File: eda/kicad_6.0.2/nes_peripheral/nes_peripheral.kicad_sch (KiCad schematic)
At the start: 126 parts, among them J1 CONN_USER, J10 CONN_JOY2, J11 CONN_JOY2_OE_SEL, J12 CONN_JOY1_OE_SEL, J13 CONN_JOY1_FC, J14 CONN_JOY1_FC_COMPATIBLE, J15 CONN_JOY1_MIC, J16 CONN_5V_RESERVE, J17 DB15_Female_JOY1, J18 DB9_Female_JOY1, J19 CONN_SOUND_IO, J2 CONN_GPIO0_DBG, J20 CONN_JOY2_FC, J21 CONN_JOY2_FC_COMPATIBLE, J22 CONN_JOY2_MIC, J23 FC_CONN, J24 CONN_CART_DBG, J25 CONN_CART_DBG, J26 DB15_Female_JOY2, J27 DB9_Female_JOY2, J28 CONN_JOY2_DBGSEL, J29 CONN_JOY1_DBGSEL, J3 CONN_GPIO1_DBG, J30 CONN_GAINSEL, J31 Screw_Terminal_SPK, J32 CONN_SPK, J33 CONN_JOY2_DBG, J34 CONN_JOY1_DBG, J4 Jack_EXT5V, J5 CONN_GPIO0_DBG, J6 CONN_GPIO1_DBG, J7 CONN_CART_OE_SEL, J8 CONN_5VSEL, J9 CONN_JOY1, U1 TXB0104PW, U10 TXB0104PW, U11 TXB0104PW, U12 TXB0104PW, U13 TXB0104PW, U14 TXB0104PW, U15 TXB0104PW, U16 TXB0104PW, U17 4021, U18 4021, U19 MAX98357, U2 TXB0104PW, U20 MAX98357, U3 TXB0104PW, U4 TXB0104PW, U5 TXB0104PW, U6 TXB0104PW, U7 TXB0104PW, U8 TXB0104PW, U9 TXB0104PW

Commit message: wip: 基板配置検討中
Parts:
- removed J13: CONN_JOY1_FC, Connector_PinSocket_2.54mm:PinSocket_2x15_P2.54mm_Vertical, symbol Connector_Generic:Conn_02x15_Odd_Even
- removed J17: DB15_Female_JOY1, Connector_Dsub:DSUB-15-HD_Female_Horizontal_P2.29x1.98mm_EdgePinOffset9.40mm, symbol Connector:DB15_Female
- removed J18: DB9_Female_JOY1, Connector_Dsub:DSUB-9_Female_Horizontal_P2.77x2.84mm_EdgePinOffset9.40mm, symbol Connector:DB9_Female
- removed J2, J5: CONN_GPIO0_DBG, Connector_PinSocket_2.54mm:PinSocket_1x20_P2.54mm_Vertical, symbol Connector_Generic:Conn_01x20
- removed J20: CONN_JOY2_FC, Connector_PinSocket_2.54mm:PinSocket_2x15_P2.54mm_Vertical, symbol Connector_Generic:Conn_02x15_Odd_Even
- removed J26: DB15_Female_JOY2, Connector_Dsub:DSUB-15-HD_Female_Horizontal_P2.29x1.98mm_EdgePinOffset9.40mm, symbol Connector:DB15_Female
- removed J27: DB9_Female_JOY2, Connector_Dsub:DSUB-9_Female_Horizontal_P2.77x2.54mm_EdgePinOffset9.40mm, symbol Connector:DB9_Female
- removed J3, J6: CONN_GPIO1_DBG, Connector_PinSocket_2.54mm:PinSocket_1x20_P2.54mm_Vertical, symbol Connector_Generic:Conn_01x20
- added H1, H2, H3: MountingHole_Pad, MountingHole:MountingHole_3.2mm_M3_Pad_TopBottom, symbol Mechanical:MountingHole_Pad
- J1: footprint Connector_PinSocket_2.54mm:PinSocket_2x06_P2.54mm_Vertical -> Connector_PinSocket_2.54mm:PinSocket_1x06_P2.54mm_Vertical; symbol Connector_Generic:Conn_02x06_Odd_Even -> Connector_Generic:Conn_01x06
- J10, J9: footprint Connector_PinSocket_2.54mm:PinSocket_2x05_P2.54mm_Vertical -> Connector_PinSocket_2.54mm:PinSocket_1x06_P2.54mm_Vertical; symbol Connector_Generic:Conn_02x05_Odd_Even -> Connector_Generic:Conn_01x06
- J2: renamed from J14; footprint Connector_PinSocket_2.54mm:PinSocket_2x09_P2.54mm_Vertical -> Connector_PinSocket_2.54mm:PinSocket_1x09_P2.54mm_Vertical; symbol Connector_Generic:Conn_02x09_Odd_Even -> Connector_Generic:Conn_01x09
- J3: renamed from J21; footprint Connector_PinSocket_2.54mm:PinSocket_2x09_P2.54mm_Vertical -> Connector_PinSocket_2.54mm:PinSocket_1x09_P2.54mm_Vertical; symbol Connector_Generic:Conn_02x09_Odd_Even -> Connector_Generic:Conn_01x09
- JP1, JP2: footprint Resistor_SMD:R_0603_1608Metric_Pad0.98x0.95mm_HandSolder -> Connector_PinSocket_2.54mm:PinSocket_2x20_P2.54mm_Vertical
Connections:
- net +5V: now also J2.6 (Pin_6), J2.7 (Pin_7), J3.6 (Pin_6), J3.7 (Pin_7); no longer J2.11 (Pin_11), J2.12 (Pin_12), J2.13 (Pin_13), J2.14 (Pin_14), J3.11 (Pin_11), J3.12 (Pin_12), J3.13 (Pin_13), J3.14 (Pin_14)
- net 3V3_JOY1_CLK: now also J9.4 (Pin_4); no longer J9.7 (Pin_7)
- net 3V3_JOY1_DO: now also J9.2 (Pin_2); no longer J9.3 (Pin_3)
- net 3V3_JOY1_P/~{S}: now also J9.3 (Pin_3); no longer J9.5 (Pin_5)
- net 3V3_JOY1_RESERVE: now also J9.5 (Pin_5); no longer J9.9 (Pin_9)
- net 3V3_JOY2_CLK: now also J10.4 (Pin_4); no longer J10.7 (Pin_7)
- net 3V3_JOY2_DO: now also J10.2 (Pin_2); no longer J10.3 (Pin_3)
- net 3V3_JOY2_MICIN: now also J10.5 (Pin_5); no longer J10.9 (Pin_9)
- net 3V3_JOY2_P/~{S}: now also J10.3 (Pin_3); no longer J10.5 (Pin_5)
- net 5V_JOY1_CLK: now also J2.4 (Pin_4); no longer J2.7 (Pin_7), J2.8 (Pin_8)
- net 5V_JOY1_DO: now also J2.2 (Pin_2); no longer J2.3 (Pin_3), J2.4 (Pin_4)
- net 5V_JOY1_P/~{S}: now also J2.3 (Pin_3); no longer J2.5 (Pin_5), J2.6 (Pin_6)
- net 5V_JOY2_CLK: now also J3.4 (Pin_4); no longer J3.7 (Pin_7), J3.8 (Pin_8)
- net 5V_JOY2_DO: now also J3.2 (Pin_2); no longer J3.3 (Pin_3), J3.4 (Pin_4)
- net 5V_JOY2_P/~{S}: now also J3.3 (Pin_3); no longer J3.5 (Pin_5), J3.6 (Pin_6)
- net GND: now also J1.2 (Pin_2), J2.8 (Pin_8), J2.9 (Pin_9), J3.8 (Pin_8), J3.9 (Pin_9), H1.1, H2.1, H3.1; no longer J1.3 (Pin_3), J1.4 (Pin_4), J10.10 (Pin_10), J10.2 (Pin_2), J10.4 (Pin_4), J10.8 (Pin_8), J2.15 (Pin_15), J2.16 (Pin_16), J2.17 (Pin_17), J2.18 (Pin_18), J3.15 (Pin_15), J3.16 (Pin_16), J3.17 (Pin_17), J3.18 (Pin_18), J9.10 (Pin_10), J9.2 (Pin_2), J9.4 (Pin_4), J9.8 (Pin_8)
- net GPIO_0_D20: now also J1.3 (Pin_3); no longer J1.5 (Pin_5), J1.6 (Pin_6)
- net GPIO_0_D21: now also J1.4 (Pin_4); no longer J1.7 (Pin_7), J1.8 (Pin_8)
- net USER_GPIO2: now also J1.5 (Pin_5); no longer J1.10 (Pin_10), J1.9 (Pin_9)
- net USER_GPIO3: now also J1.6 (Pin_6); no longer J1.11 (Pin_11), J1.12 (Pin_12)
- no-connect marks 72 -> 9
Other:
- moved on the sheet: D1, D2, D3, F1, J4, J7, J8, R1, R2, R3, R4

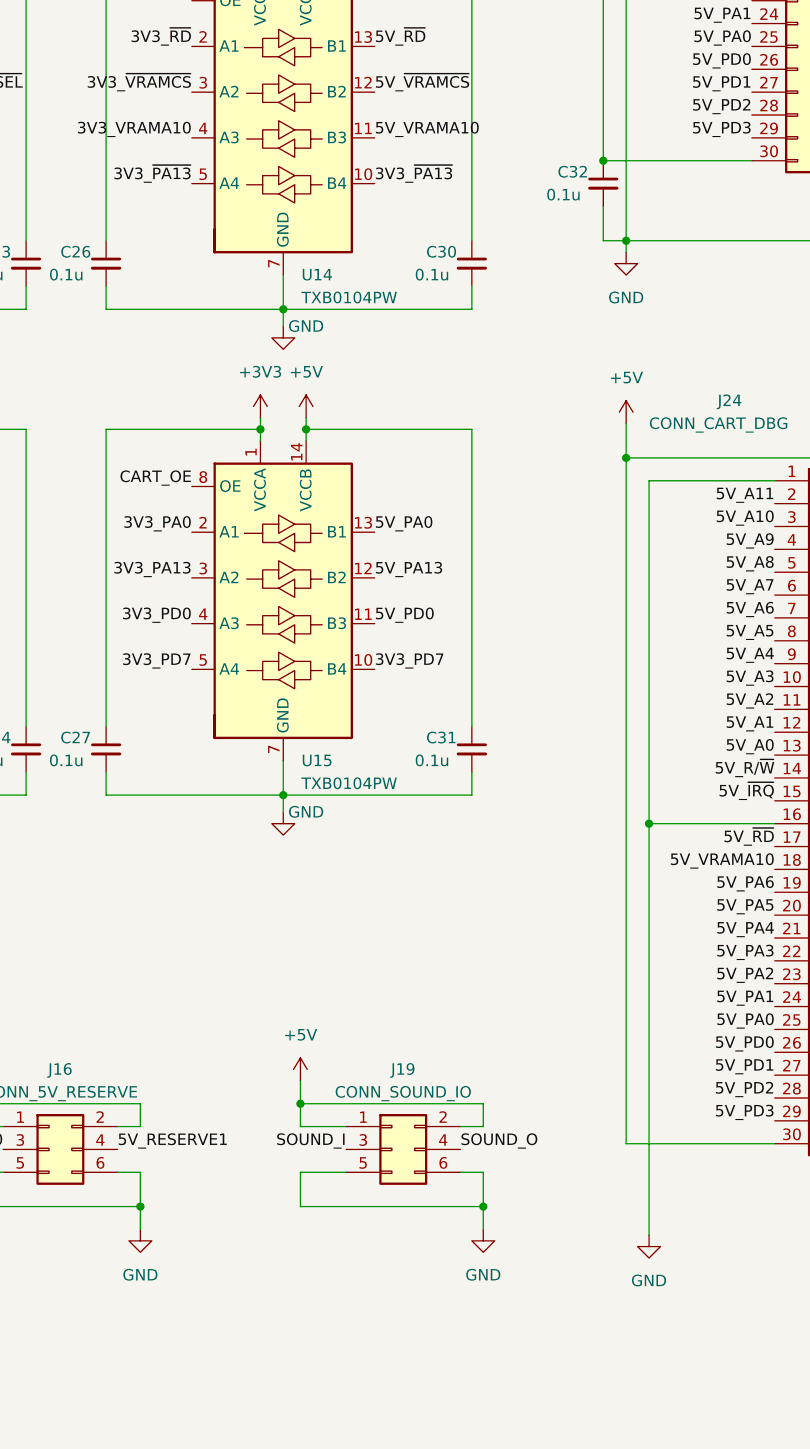
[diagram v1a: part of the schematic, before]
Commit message: feat: レベル変換回路配線中
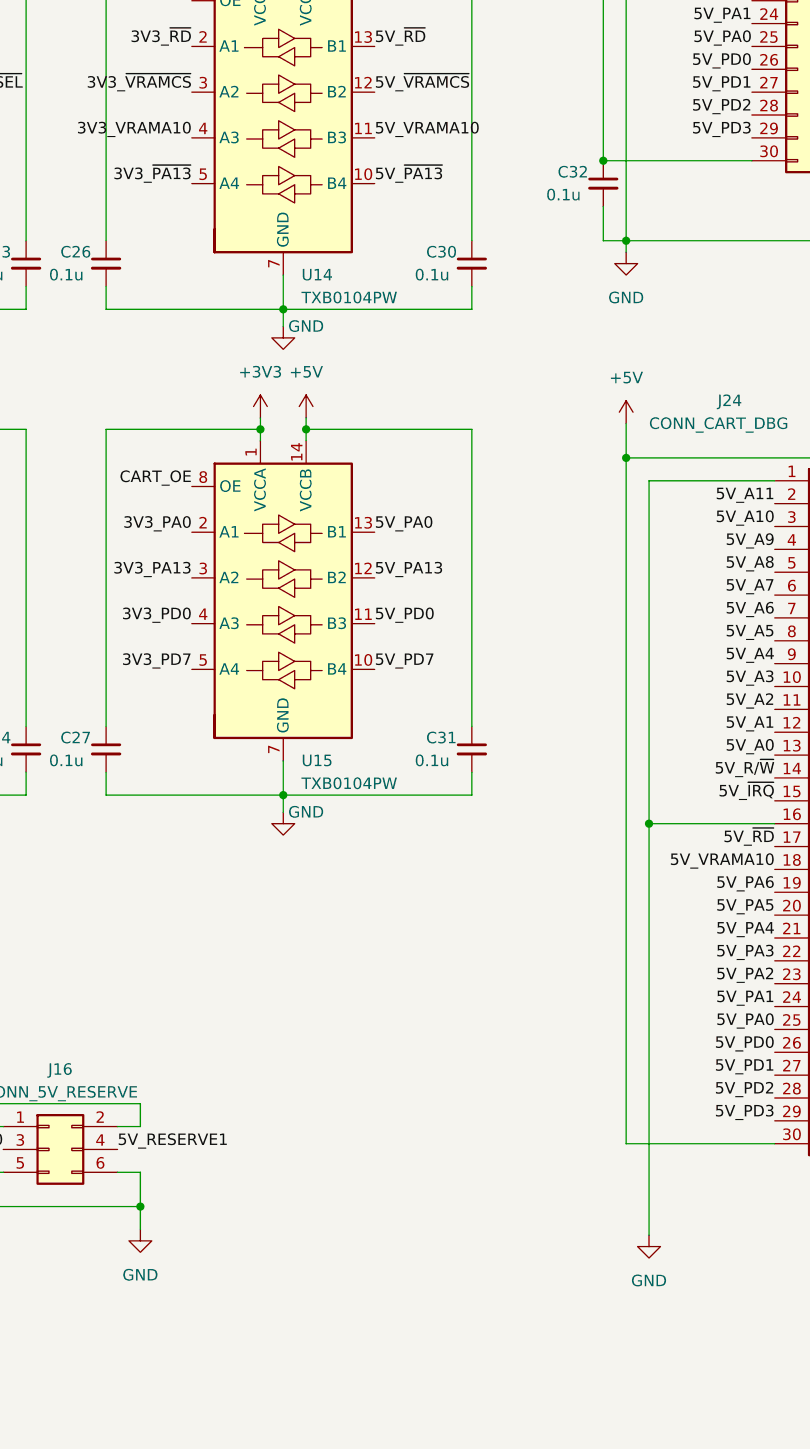
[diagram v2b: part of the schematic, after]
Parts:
- removed J19: CONN_SOUND_IO, Connector_PinSocket_2.54mm:PinSocket_2x03_P2.54mm_Vertical, symbol Connector_Generic:Conn_02x03_Odd_Even
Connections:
- net 3V3_PD7: no longer U15.10 (B4)
- net 3V3_~{PA13}: no longer U14.10 (B4)
- net 5V_PD7: now also U15.10 (B4)
- net 5V_~{PA13}: now also U14.10 (B4)
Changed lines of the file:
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@@
   (junction (at 481.584 304.292) (diameter 0) (color 0 0 0 0)
   )
-  (junction (at 334.01 212.725) (diameter 0) (color 0 0 0 0)
-  )
   (junction (at 334.645 29.21) (diameter 0) (color 0 0 0 0)
   )
@@
   (junction (at 256.54 302.895) (diameter 0) (color 0 0 0 0)
   )
-  (junction (at 354.33 224.155) (diameter 0) (color 0 0 0 0)
-  )
   (junction (at 237.109 337.439) (diameter 0) (color 0 0 0 0)
   )
@@
     (stroke (width 0) (type default) (color 0 0 0 0))
   )
-  (wire (pts (xy 351.79 220.345) (xy 354.33 220.345))
-    (stroke (width 0) (type default) (color 0 0 0 0))
-  )
   (wire (pts (xy 162.56 178.435) (xy 162.56 175.895))
     (stroke (width 0) (type default) (color 0 0 0 0))
@@
     (stroke (width 0) (type default) (color 0 0 0 0))
   )
-  (wire (pts (xy 334.01 220.345) (xy 334.01 224.155))
-    (stroke (width 0) (type default) (color 0 0 0 0))
-  )
   (wire (pts (xy 282.575 174.625) (xy 282.575 178.435))
     (stroke (width 0) (type default) (color 0 0 0 0))
@@
     (stroke (width 0) (type default) (color 0 0 0 0))
   )
-  (wire (pts (xy 354.33 212.725) (xy 354.33 215.265))
-    (stroke (width 0) (type default) (color 0 0 0 0))
-  )
   (wire (pts (xy 570.23 289.306) (xy 570.23 291.846))
     (stroke (width 0) (type default) (color 0 0 0 0))
@@
     (stroke (width 0) (type default) (color 0 0 0 0))
   )
-  (wire (pts (xy 334.01 215.265) (xy 339.09 215.265))
-    (stroke (width 0) (type default) (color 0 0 0 0))
-  )
   (wire (pts (xy 124.46 144.78) (xy 124.46 143.764))
     (stroke (width 0) (type default) (color 0 0 0 0))
@@
     (stroke (width 0) (type default) (color 0 0 0 0))
   )
-  (wire (pts (xy 354.33 224.155) (xy 354.33 226.695))
-    (stroke (width 0) (type default) (color 0 0 0 0))
-  )
   (wire (pts (xy 354.33 301.625) (xy 375.285 301.625))
     (stroke (width 0) (type default) (color 0 0 0 0))
@@
     (stroke (width 0) (type default) (color 0 0 0 0))
   )
-  (wire (pts (xy 334.01 210.185) (xy 334.01 212.725))
-    (stroke (width 0) (type default) (color 0 0 0 0))
-  )
   (wire (pts (xy 184.785 190.5) (xy 184.785 191.77))
     (stroke (width 0) (type default) (color 0 0 0 0))
@@
     (stroke (width 0) (type default) (color 0 0 0 0))
   )
-  (wire (pts (xy 354.33 215.265) (xy 351.79 215.265))
-    (stroke (width 0) (type default) (color 0 0 0 0))
-  )
   (wire (pts (xy 526.415 36.195) (xy 528.955 36.195))
     (stroke (width 0) (type default) (color 0 0 0 0))
   )
-  (wire (pts (xy 334.01 212.725) (xy 334.01 215.265))
-    (stroke (width 0) (type default) (color 0 0 0 0))
-  )
   (wire (pts (xy 52.705 132.08) (xy 66.04 132.08))
     (stroke (width 0) (type default) (color 0 0 0 0))
@@
     (stroke (width 0) (type default) (color 0 0 0 0))
   )
-  (wire (pts (xy 334.01 224.155) (xy 354.33 224.155))
-    (stroke (width 0) (type default) (color 0 0 0 0))
-  )
   (wire (pts (xy 549.275 123.19) (xy 545.465 123.19))
     (stroke (width 0) (type default) (color 0 0 0 0))
@@
     (stroke (width 0) (type default) (color 0 0 0 0))
   )
-  (wire (pts (xy 334.01 212.725) (xy 354.33 212.725))
-    (stroke (width 0) (type default) (color 0 0 0 0))
-  )
   (wire (pts (xy 459.105 124.46) (xy 473.075 124.46))
     (stroke (width 0) (type default) (color 0 0 0 0))
@@
     (stroke (width 0) (type default) (color 0 0 0 0))
   )
-  (wire (pts (xy 354.33 220.345) (xy 354.33 224.155))
-    (stroke (width 0) (type default) (color 0 0 0 0))
-  )
   (wire (pts (xy 370.205 72.39) (xy 370.205 116.84))
     (stroke (width 0) (type default) (color 0 0 0 0))
@@
     (stroke (width 0) (type default) (color 0 0 0 0))
   )
-  (wire (pts (xy 339.09 220.345) (xy 334.01 220.345))
-    (stroke (width 0) (type default) (color 0 0 0 0))
-  )
   (wire (pts (xy 124.46 101.6) (xy 124.46 124.46))
     (stroke (width 0) (type default) (color 0 0 0 0))
@@
     (effects (font (size 1.27 1.27)) (justify right bottom))
   )
-  (label "3V3_~{PA13}" (at 342.265 110.49 0)
+  (label "5V_~{PA13}" (at 342.265 110.49 0)
     (effects (font (size 1.27 1.27)) (justify left bottom))
   )
@@
     (effects (font (size 1.27 1.27)) (justify left bottom))
   )
-  (label "SOUND_O" (at 351.79 217.805 0)
-    (effects (font (size 1.27 1.27)) (justify left bottom))
-  )
   (label "JOY1_3V3_DBG_D3" (at 550.164 279.146 180)
     (effects (font (size 1.27 1.27)) (justify right bottom))
@@
     (effects (font (size 1.27 1.27)) (justify right bottom))
   )
-  (label "SOUND_I" (at 339.09 217.805 180)
-    (effects (font (size 1.27 1.27)) (justify right bottom))
-  )
   (label "5V_PA8" (at 399.415 194.31 0)
     (effects (font (size 1.27 1.27)) (justify left bottom))
@@
     (effects (font (size 1.27 1.27)) (justify left bottom))
   )
-  (label "3V3_PD7" (at 342.265 164.465 0)
+  (label "5V_PD7" (at 342.265 164.465 0)
     (effects (font (size 1.27 1.27)) (justify left bottom))
   )
@@
     (pin "9")
   )
-  (symbol (lib_id "Connector_Generic:Conn_02x03_Odd_Even") (at 344.17 217.805 0) (unit 1)
-    (in_bom yes) (on_board yes) (fields_autoplaced)
-    (property "Reference" "J19" (id 0) (at 345.44 208.915 0))
-    (property "Value" "CONN_SOUND_IO" (id 1) (at 345.44 211.455 0))
-    (property "Footprint" "Connector_PinSocket_2.54mm:PinSocket_2x03_P2.54mm_Vertical" (id 2) (at 344.17 217.805 0)
-      (effects (font (size 1.27 1.27)) hide)
-    )
-    (property "Datasheet" "~" (id 3) (at 344.17 217.805 0)
-      (effects (font (size 1.27 1.27)) hide)
-    )
-    (pin "1")
-    (pin "2")
-    (pin "3")
-    (pin "4")
-    (pin "5")
-    (pin "6")
-  )
   (symbol (lib_id "Device:R_Small") (at 47.498 192.278 0) (unit 1)
     (in_bom yes) (on_board yes)
@@
     (pin "1")
   )
-  (symbol (lib_id "power:GND") (at 354.33 226.695 0) (unit 1)
-    (in_bom yes) (on_board yes) (fields_autoplaced)
-    (property "Reference" "#PWR0146" (id 0) (at 354.33 233.045 0)
-      (effects (font (size 1.27 1.27)) hide)
-    )
-    (property "Value" "GND" (id 1) (at 354.33 231.775 0))
-    (property "Footprint" "" (id 2) (at 354.33 226.695 0)
-      (effects (font (size 1.27 1.27)) hide)
-    )
-    (property "Datasheet" "" (id 3) (at 354.33 226.695 0)
-      (effects (font (size 1.27 1.27)) hide)
-    )
-    (pin "1")
-  )
   (symbol (lib_id "Logic_LevelTranslator:TXB0104PW") (at 182.245 156.845 0) (unit 1)
     (in_bom yes) (on_board yes) (fields_autoplaced)
@@
     (pin "1")
   )
-  (symbol (lib_id "power:+5V") (at 334.01 210.185 0) (unit 1)
-    (in_bom yes) (on_board yes) (fields_autoplaced)
-    (property "Reference" "#PWR0147" (id 0) (at 334.01 213.995 0)
-      (effects (font (size 1.27 1.27)) hide)
-    )
-    (property "Value" "+5V" (id 1) (at 334.01 205.105 0))
-    (property "Footprint" "" (id 2) (at 334.01 210.185 0)
-      (effects (font (size 1.27 1.27)) hide)
-    )
-    (property "Datasheet" "" (id 3) (at 334.01 210.185 0)
-      (effects (font (size 1.27 1.27)) hide)
-    )
-    (pin "1")
-  )
   (symbol (lib_id "power:GND") (at 256.54 304.8 0) (unit 1)
     (in_bom yes) (on_board yes)
@@
       (reference "#PWR0145") (unit 1) (value "+5V") (footprint "")
     )
-    (path "/1ea3e8ed-57d7-458c-b8cf-35ca6b8a7141"
-      (reference "#PWR0146") (unit 1) (value "GND") (footprint "")
-    )
-    (path "/752c90af-d425-4803-912c-e30c21c0145a"
-      (reference "#PWR0147") (unit 1) (value "+5V") (footprint "")
-    )
     (path "/3c530095-3c6e-41b9-89e4-5cf6b10f3c67"
       (reference "#PWR0148") (unit 1) (value "+5V") (footprint "")
@@
       (reference "J16") (unit 1) (value "CONN_5V_RESERVE") (footprint "Connector_PinSocket_2.54mm:PinSocket_2x03_P2.54mm_Vertical")
     )
-    (path "/0ba8fe54-6693-4c44-87c0-51fe94533bce"
-      (reference "J19") (unit 1) (value "CONN_SOUND_IO") (footprint "Connector_PinSocket_2.54mm:PinSocket_2x03_P2.54mm_Vertical")
-    )
     (path "/c4dc6e3d-4b17-41f3-823a-1bacf93cf868"

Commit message: feat: 残りの部品配置を修正中
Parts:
- removed J32: CONN_SPK, Resistor_SMD:R_0603_1608Metric_Pad0.98x0.95mm_HandSolder, symbol Connector_Generic:Conn_02x03_Odd_Even
- J11, J12, J7, J8: footprint Connector_PinSocket_2.54mm:PinSocket_1x03_P2.54mm_Vertical -> Connector_PinHeader_2.54mm:PinHeader_1x03_P2.54mm_Vertical
- J15, J22: footprint Connector_PinSocket_2.54mm:PinSocket_2x01_P2.54mm_Vertical -> Connector_PinSocket_2.54mm:PinSocket_1x02_P2.54mm_Vertical
- J28, J29: footprint Connector_PinSocket_2.54mm:PinSocket_2x01_P2.54mm_Vertical -> Connector_PinHeader_2.54mm:PinHeader_1x02_P2.54mm_Vertical
- J30: footprint Connector_PinSocket_2.54mm:PinSocket_2x05_P2.54mm_Vertical -> Connector_PinHeader_2.54mm:PinHeader_2x05_P2.54mm_Vertical
- J33, J34: footprint Resistor_SMD:R_0603_1608Metric_Pad0.98x0.95mm_HandSolder -> Connector_PinSocket_2.54mm:PinSocket_2x07_P2.54mm_Vertical
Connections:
- net 5V_JOY1_RESERVE: now also U9.10 (B4)
- net 5V_JOY2_MICIN: now also U16.10 (B4)
- net GND: now also J15.2 (Pin_2), J22.2 (Pin_2)
- net JOY1_3V3_DBG_D0: now also J34.15 (Pin_15); no longer J34.1 (Pin_1)
- net JOY1_3V3_DBG_D1: now also J34.13 (Pin_13); no longer J34.3 (Pin_3)
- net JOY1_3V3_DBG_D2: now also J34.11 (Pin_11); no longer J34.5 (Pin_5)
- net JOY1_3V3_DBG_D3: now also J34.9 (Pin_9); no longer J34.7 (Pin_7)
- net JOY1_3V3_DBG_D4: now also J34.7 (Pin_7); no longer J34.9 (Pin_9)
- net JOY1_3V3_DBG_D5: now also J34.5 (Pin_5); no longer J34.11 (Pin_11)
- net JOY1_3V3_DBG_D6: now also J34.3 (Pin_3); no longer J34.13 (Pin_13)
- net JOY1_3V3_DBG_D7: now also J34.1 (Pin_1); no longer J34.15 (Pin_15)
- net JOY2_3V3_DBG_D0: now also J33.15 (Pin_15); no longer J33.1 (Pin_1)
- net JOY2_3V3_DBG_D1: now also J33.13 (Pin_13); no longer J33.3 (Pin_3)
- net JOY2_3V3_DBG_D2: now also J33.11 (Pin_11); no longer J33.5 (Pin_5)
- net JOY2_3V3_DBG_D3: now also J33.9 (Pin_9); no longer J33.7 (Pin_7)
- net JOY2_3V3_DBG_D4: now also J33.7 (Pin_7); no longer J33.9 (Pin_9)
- net JOY2_3V3_DBG_D5: now also J33.5 (Pin_5); no longer J33.11 (Pin_11)
- net JOY2_3V3_DBG_D6: now also J33.3 (Pin_3); no longer J33.13 (Pin_13)
- net JOY2_3V3_DBG_D7: now also J33.1 (Pin_1); no longer J33.15 (Pin_15)
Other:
- moved on the sheet: J15, J22
